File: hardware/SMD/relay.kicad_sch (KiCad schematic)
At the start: 7 parts, among them J1 Screw_Terminal_01x03, J4 Screw_Terminal_01x03, J5 Screw_Terminal_01x03, K1 G6K-2F-Y-TR DC12, K2 G6K-2F-Y-TR DC12

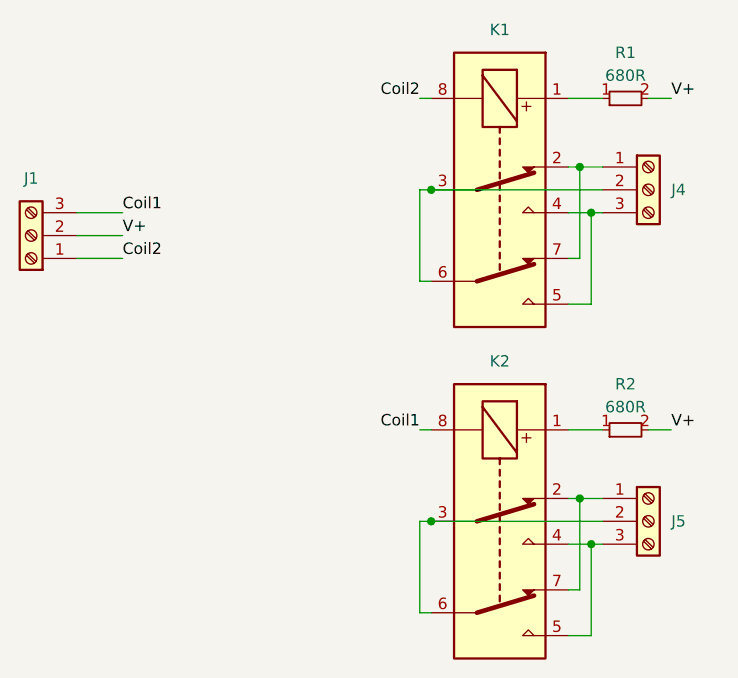
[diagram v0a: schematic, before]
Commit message: added data to readme.md
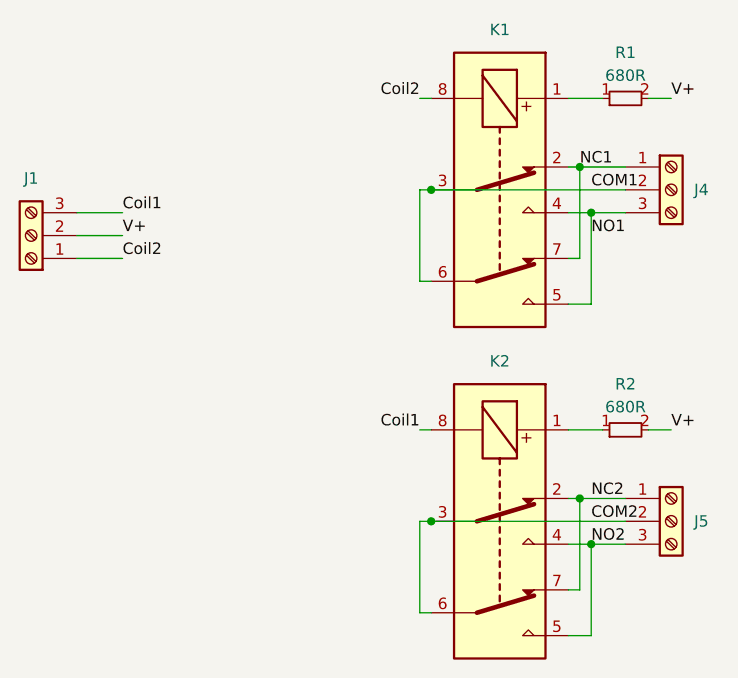
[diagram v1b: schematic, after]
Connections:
- net NC1: now reaches J4.1 (Pin_1), K1.2, K1.7
- net COM1: now reaches J4.2 (Pin_2), K1.3, K1.6
- net NO1: now reaches J4.3 (Pin_3), K1.4, K1.5
- net NC2: now reaches J5.1 (Pin_1), K2.2, K2.7
- net COM2: now reaches J5.2 (Pin_2), K2.3, K2.6
- net NO2: now reaches J5.3 (Pin_3), K2.4, K2.5
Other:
- moved on the sheet: J4, J5
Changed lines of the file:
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@@
 	(wire
 		(pts
-			(xy 165.1 102.87) (xy 166.37 102.87)
+			(xy 165.1 102.87) (xy 168.91 102.87)
 		)
 		(stroke
@@
 	(wire
 		(pts
+			(xy 165.1 102.87) (xy 165.1 113.03)
+		)
+		(stroke
+			(width 0)
+			(type default)
+		)
+	)
+	(wire
+		(pts
+			(xy 162.56 113.03) (xy 165.1 113.03)
+		)
+		(stroke
+			(width 0)
+			(type default)
+		)
+	)
+	(wire
+		(pts
+			(xy 107.95 71.12) (xy 113.03 71.12)
+		)
+		(stroke
+			(width 0)
+			(type default)
+		)
+	)
+	(wire
+		(pts
+			(xy 147.32 73.66) (xy 146.05 73.66)
+		)
+		(stroke
+			(width 0)
+			(type default)
+		)
+	)
+	(wire
+		(pts
+			(xy 165.1 66.04) (xy 165.1 76.2)
+		)
+		(stroke
+			(width 0)
+			(type default)
+		)
+	)
+	(wire
+		(pts
+			(xy 146.05 63.5) (xy 147.32 63.5)
+		)
+		(stroke
+			(width 0)
+			(type default)
+		)
+	)
+	(wire
+		(pts
+			(xy 163.83 97.79) (xy 163.83 107.95)
+		)
+		(stroke
+			(width 0)
+			(type default)
+		)
+	)
+	(wire
+		(pts
 			(xy 163.83 60.96) (xy 163.83 71.12)
 		)
@@
 	(wire
 		(pts
-			(xy 165.1 102.87) (xy 165.1 113.03)
-		)
-		(stroke
-			(width 0)
-			(type default)
-		)
-	)
-	(wire
-		(pts
-			(xy 162.56 113.03) (xy 165.1 113.03)
-		)
-		(stroke
-			(width 0)
-			(type default)
-		)
-	)
-	(wire
-		(pts
-			(xy 107.95 71.12) (xy 113.03 71.12)
-		)
-		(stroke
-			(width 0)
-			(type default)
-		)
-	)
-	(wire
-		(pts
-			(xy 147.32 73.66) (xy 146.05 73.66)
-		)
-		(stroke
-			(width 0)
-			(type default)
-		)
-	)
-	(wire
-		(pts
-			(xy 165.1 66.04) (xy 165.1 76.2)
-		)
-		(stroke
-			(width 0)
-			(type default)
-		)
-	)
-	(wire
-		(pts
-			(xy 146.05 63.5) (xy 147.32 63.5)
-		)
-		(stroke
-			(width 0)
-			(type default)
-		)
-	)
-	(wire
-		(pts
-			(xy 163.83 97.79) (xy 163.83 107.95)
-		)
-		(stroke
-			(width 0)
-			(type default)
-		)
-	)
-	(wire
-		(pts
 			(xy 173.99 53.34) (xy 171.45 53.34)
 		)
@@
 	(wire
 		(pts
-			(xy 163.83 97.79) (xy 166.37 97.79)
-		)
-		(stroke
-			(width 0)
-			(type default)
-		)
-	)
-	(wire
-		(pts
-			(xy 163.83 60.96) (xy 166.37 60.96)
-		)
-		(stroke
-			(width 0)
-			(type default)
-		)
-	)
-	(wire
-		(pts
-			(xy 165.1 66.04) (xy 166.37 66.04)
+			(xy 163.83 97.79) (xy 168.91 97.79)
+		)
+		(stroke
+			(width 0)
+			(type default)
+		)
+	)
+	(wire
+		(pts
+			(xy 163.83 60.96) (xy 168.91 60.96)
+		)
+		(stroke
+			(width 0)
+			(type default)
+		)
+	)
+	(wire
+		(pts
+			(xy 165.1 66.04) (xy 168.91 66.04)
 		)
 		(stroke
@@
 	(wire
 		(pts
-			(xy 147.32 100.33) (xy 166.37 100.33)
+			(xy 147.32 100.33) (xy 168.91 100.33)
 		)
 		(stroke
@@
 	(wire
 		(pts
-			(xy 147.32 63.5) (xy 166.37 63.5)
-		)
-		(stroke
-			(width 0)
-			(type default)
+			(xy 147.32 63.5) (xy 168.91 63.5)
+		)
+		(stroke
+			(width 0)
+			(type default)
+		)
+	)
+	(label "NO1"
+		(at 165.1 68.58 0)
+		(fields_autoplaced yes)
+		(effects
+			(font
+				(size 1.27 1.27)
+			)
+			(justify left bottom)
+		)
+	)
+	(label "NC2"
+		(at 165.1 97.79 0)
+		(fields_autoplaced yes)
+		(effects
+			(font
+				(size 1.27 1.27)
+			)
+			(justify left bottom)
 		)
 	)
 	(label "V+"
 		(at 173.99 53.34 0)
+		(fields_autoplaced yes)
 		(effects
 			(font
@@
 	(label "Coil2"
 		(at 113.03 71.12 0)
+		(fields_autoplaced yes)
 		(effects
 			(font
@@
 	(label "Coil2"
 		(at 146.05 53.34 180)
+		(fields_autoplaced yes)
 		(effects
 			(font
@@
 	(label "Coil1"
 		(at 113.03 66.04 0)
+		(fields_autoplaced yes)
 		(effects
 			(font
@@
 	(label "V+"
 		(at 113.03 68.58 0)
+		(fields_autoplaced yes)
+		(effects
+			(font
+				(size 1.27 1.27)
+			)
+			(justify left bottom)
+		)
+	)
+	(label "COM1"
+		(at 165.1 63.5 0)
+		(fields_autoplaced yes)
 		(effects
 			(font
@@
 	(label "V+"
 		(at 173.99 90.17 0)
+		(fields_autoplaced yes)
+		(effects
+			(font
+				(size 1.27 1.27)
+			)
+			(justify left bottom)
+		)
+	)
+	(label "NO2"
+		(at 165.1 102.87 0)
+		(fields_autoplaced yes)
+		(effects
+			(font
+				(size 1.27 1.27)
+			)
+			(justify left bottom)
+		)
+	)
+	(label "NC1"
+		(at 163.83 60.96 0)
+		(fields_autoplaced yes)
 		(effects
 			(font
@@
 	(label "Coil1"
 		(at 146.05 90.17 180)
+		(fields_autoplaced yes)
 		(effects
 			(font
@@
 			)
 			(justify right bottom)
+		)
+	)
+	(label "COM2"
+		(at 165.1 100.33 0)
+		(fields_autoplaced yes)
+		(effects
+			(font
+				(size 1.27 1.27)
+			)
+			(justify left bottom)
 		)
 	)
@@
 	(symbol
 		(lib_id "Connector:Screw_Terminal_01x03")
-		(at 171.45 100.33 0)
+		(at 173.99 100.33 0)
 		(unit 1)
 		(exclude_from_sim no)
@@
 		(fields_autoplaced yes)
 		(property "Reference" "J5"
-			(at 173.99 100.3299 0)
+			(at 176.53 100.3299 0)
 			(effects
 				(font
@@
 		)
 		(property "Value" "Screw_Terminal_01x03"
-			(at 171.45 106.68 0)
+			(at 173.99 106.68 0)
 			(effects
 				(font
@@
 		)
 		(property "Footprint" "Connector_Phoenix_MC:PhoenixContact_MCV_1,5_3-G-3.5_1x03_P3.50mm_Vertical"
-			(at 171.45 100.33 0)
+			(at 173.99 100.33 0)
 			(effects
 				(font
@@
 		)
 		(property "Datasheet" "~"
-			(at 171.45 100.33 0)
+			(at 173.99 100.33 0)
 			(effects
 				(font
@@
 		)
 		(property "Description" "Generic screw terminal, single row, 01x03, script generated (kicad-library-utils/schlib/autogen/connector/)"
-			(at 171.45 100.33 0)
+			(at 173.99 100.33 0)
 			(effects
 				(font
@@
 		)
 		(property "JLCPCB Part#" "C192778"
-			(at 171.45 100.33 0)
+			(at 173.99 100.33 0)
 			(effects
 				(font
@@
 		)
 		(property "Mating Part#" "C560231"
-			(at 171.45 100.33 0)
+			(at 173.99 100.33 0)
 			(effects
 				(font
@@
 	(symbol
 		(lib_id "Connector:Screw_Terminal_01x03")
-		(at 171.45 63.5 0)
+		(at 173.99 63.5 0)
 		(unit 1)
 		(exclude_from_sim no)
@@
 		(fields_autoplaced yes)
 		(property "Reference" "J4"
-			(at 173.99 63.4999 0)
+			(at 176.53 63.4999 0)
 			(effects
 				(font
@@
 		)
 		(property "Value" "Screw_Terminal_01x03"
-			(at 171.45 69.85 0)
+			(at 173.99 69.85 0)
 			(effects
 				(font
@@
 		)
 		(property "Footprint" "Connector_Phoenix_MC:PhoenixContact_MC_1,5_3-G-3.5_1x03_P3.50mm_Horizontal"
-			(at 171.45 63.5 0)
+			(at 173.99 63.5 0)
 			(effects
 				(font
@@
 		)
 		(property "Datasheet" "~"
-			(at 171.45 63.5 0)
+			(at 173.99 63.5 0)
 			(effects
 				(font
@@
 		)
 		(property "Description" "Generic screw terminal, single row, 01x03, script generated (kicad-library-utils/schlib/autogen/connector/)"
-			(at 171.45 63.5 0)
+			(at 173.99 63.5 0)
 			(effects
 				(font
@@
 		)
 		(property "JLCPCB Part#" "C22380440"
-			(at 171.45 63.5 0)
-			(effects
-				(font
+			(at 173.99 63.5 0)
+			(effects
+				(font
